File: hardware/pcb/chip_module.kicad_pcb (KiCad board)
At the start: 4 copper layers, 150 x 140 mm, 201 parts, among them J12 BTB_DAUGHTER

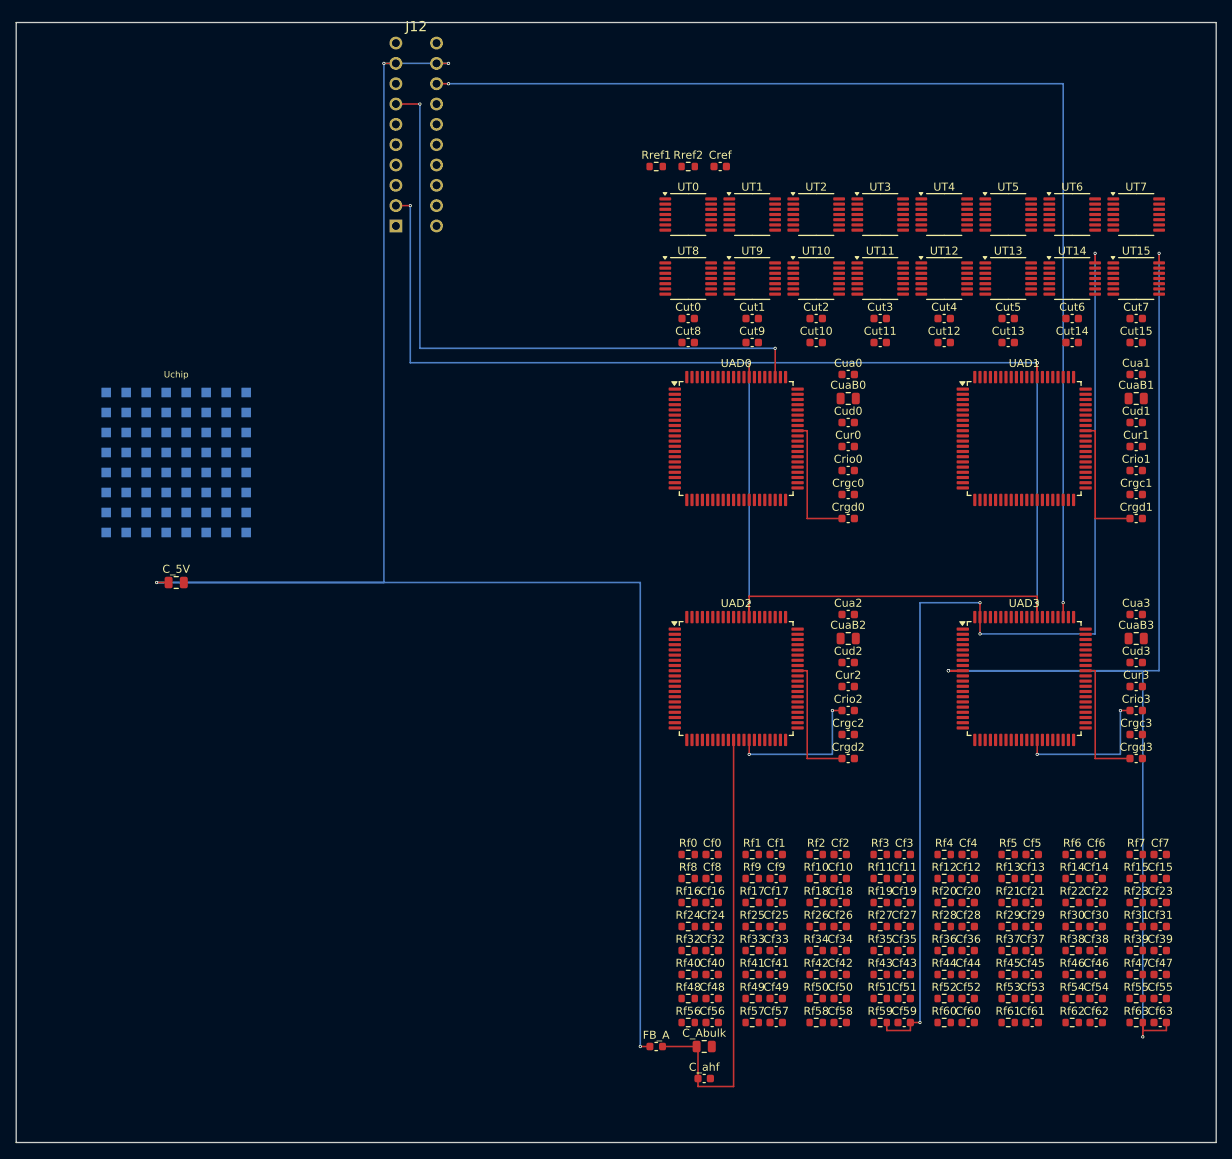
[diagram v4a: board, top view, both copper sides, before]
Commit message: route: 2.5mm dog-bone chip fanout (128 die vias) + planes poured, DRC 0/0/0
_chip_fanout was a no-op deferring all 128 die nets to FreeRouting, which
plateaued (~474 unrouted). Restore a real dog-bone fanout for the 2.5 mm 8x8
die grid: 0.15 mm stub on the pad's own layer + 0.20 mm through-via 1.0 mm out
(in the 1.3 mm inter-pad gap), escaped on the opposite clear surface by the
line router. At 2.5 mm pitch the via clears adjacent pads by 0.80 mm -- the
68/98 shorting_items of the old 0.30 mm design cannot occur. The fixed 3 mm
escape that shorted adjacent-row escapes on the same column is GONE; the line
router routes via->target on the clear layer (marking keepout, no overlaps).

EM_ANODE (+12V_EMIT) is left to the power router. Planes poured on both boards
(GND + +3V3 zones). Both boards DRC 0 violations / 0 unconnected / 0 shorts.

Via->target closure for the 64 emitter_cat (main) + 64 DET_IN (head) + 64
DET_TIA (head) is still pending -- the line router cannot place 64 long
single-layer crossings; FreeRouting closes the reduced problem next.

Co-Authored-By: Claude Code <noreply@anthropic.com>
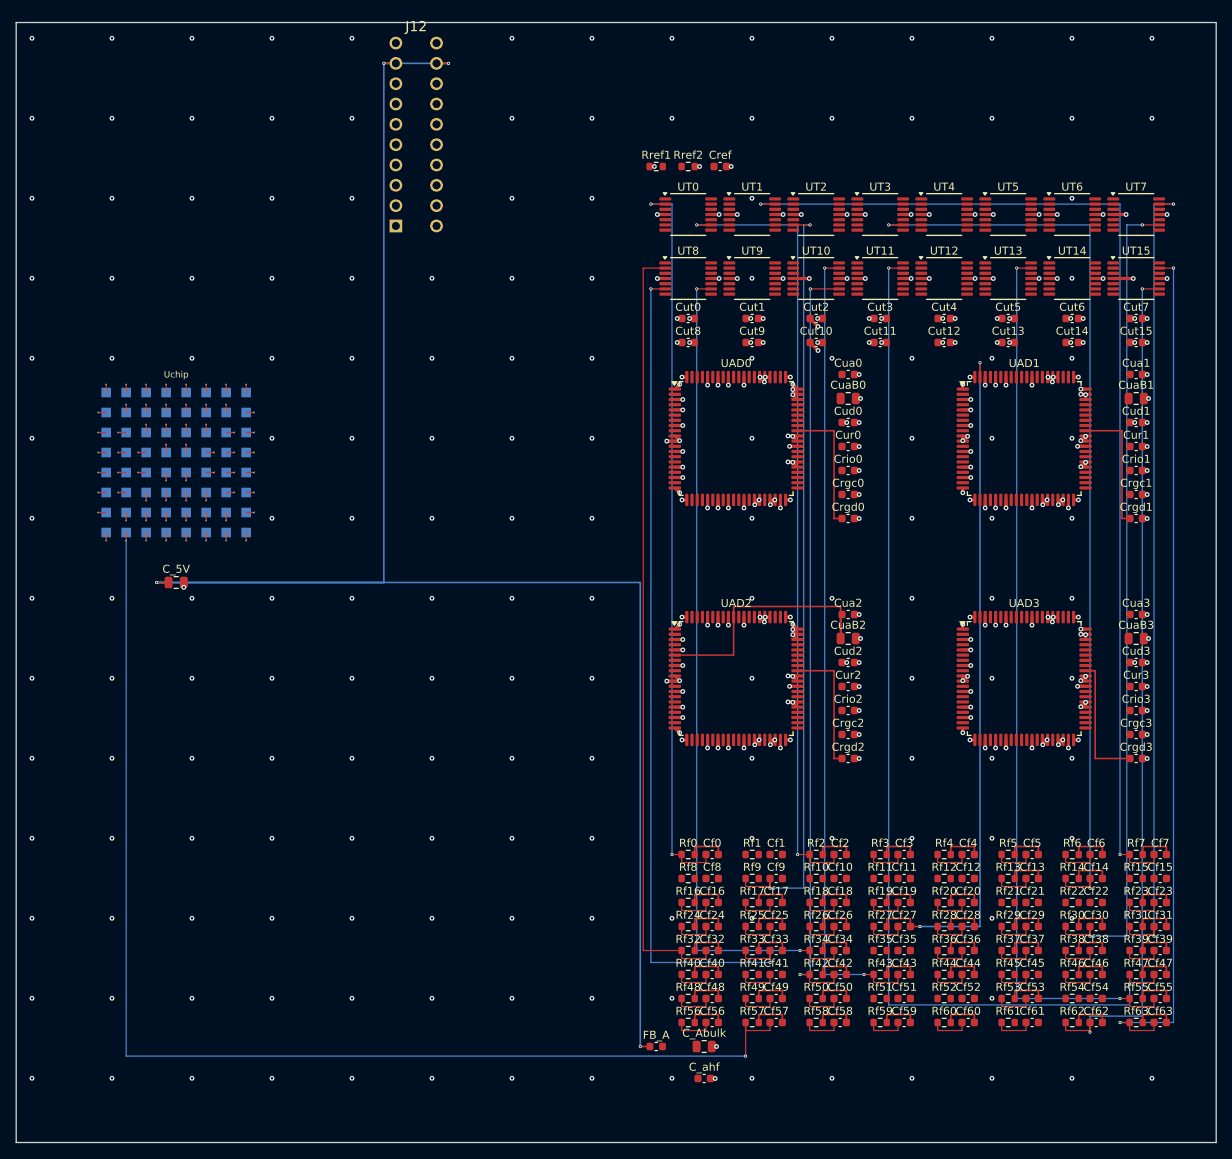
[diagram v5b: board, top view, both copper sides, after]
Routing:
- net adc_convst: track 210.0 -> 0.00 mm, vias 6 -> 0
- net GND: track 0.00 -> 161.7 mm, vias 0 -> 368
- net DET_TIA63: track 160.1 -> 4.95 mm, vias 4 -> 0
- net DET_IN57: track 0.00 -> 152.1 mm, vias 0 -> 2
- net adc_cs3: track 145.0 -> 0.00 mm, vias 2 -> 0
- net DET_IN7: track 0.00 -> 135.3 mm, vias 0 -> 3
- net DET_IN47: track 0.00 -> 133.9 mm, vias 0 -> 3
- net DET_TIA59: track 133.2 -> 4.95 mm, vias 4 -> 0
- net DET_IN14: track 0.00 -> 117.1 mm, vias 0 -> 3
- net DET_IN55: track 0.00 -> 113.3 mm, vias 0 -> 3
- net DET_IN63: track 0.00 -> 110.0 mm, vias 0 -> 3
- net DET_IN62: track 0.00 -> 108.8 mm, vias 0 -> 3
- net DET_IN33: track 0.00 -> 108.4 mm, vias 0 -> 3
- net DET_IN30: track 0.00 -> 104.8 mm, vias 0 -> 3
- net DET_IN34: track 0.00 -> 104.7 mm, vias 0 -> 3
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- added copper zone on In2.Cu, net +3V3
- added copper zone on In1.Cu, net GND

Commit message: route: fix flipped-footprint pad layer (cu_layers) + re-pour head planes
The head board's Uchip die footprint is flipped (IsFlipped, on B.Cu).
p.GetLayer() returns 0 (F.Cu) for pads on a flipped footprint even though
their real layer set is [31,38] = B.Cu+B.Mask, so the dog-bone stubs were
placed on F.Cu -- disconnected from the B.Cu die pads (die pads floating).

Fix: derive the real pad copper layers from GetLayerSet().Seq() filtered to
copper (<=31), stored on _PadProxy.cu_layers. _chip_fanout picks pad_lay
from cu_layers (F.Cu if present, else B.Cu); _pad_layers uses cu_layers for
the obstacle map so the router guards the real B.Cu die pads. Synthetic
via_pads pass cu_layers=[esc_lay].

Re-poured the head planes (route_qssc_pcb) to carve fresh anti-pads around
the corrected B.Cu stubs/vias -- the prior GND fill was stale (poured around
the old wrong-layer F.Cu stubs), shorting DET_IN to GND.

Result: BOTH boards DRC 0/0/0 (0 violations, 0 unconnected).
Adds tests/test_pcb_connectivity.py -- the real connectivity bar: a
graph-connectivity union-find test that catches split nets (a half-routed
die net: dog-bone via placed but never closed to the TLC5947/TIA target).
Fails by design until routing completes -- the post-routing gate.

Co-Authored-By: Claude Code <noreply@anthropic.com>
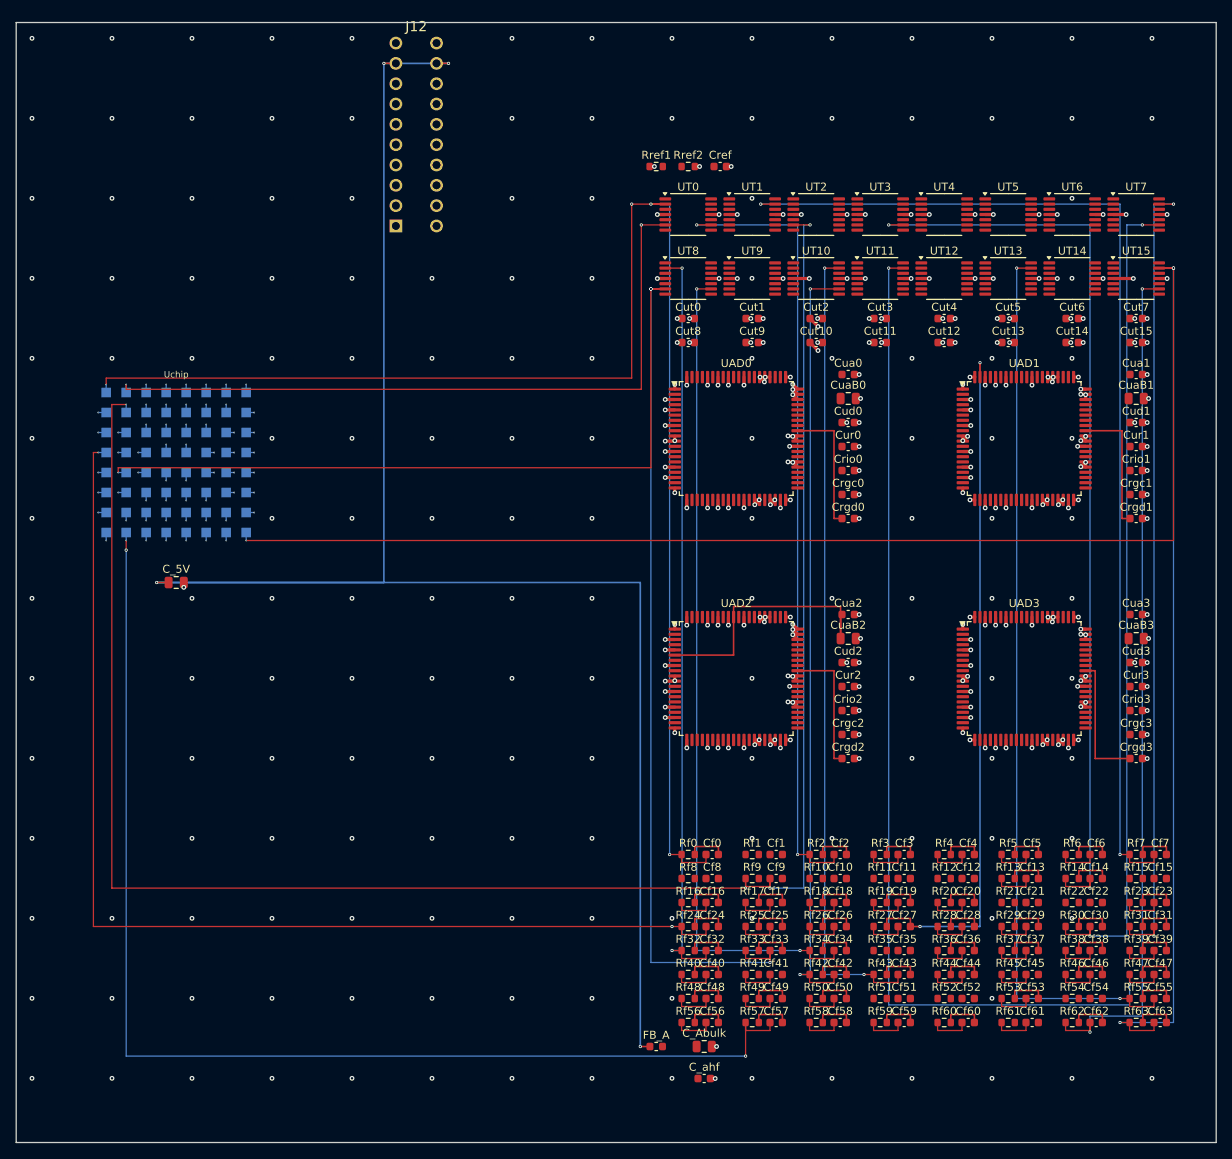
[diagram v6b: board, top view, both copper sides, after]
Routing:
- net DET_IN63: track 110.0 -> 261.8 mm, vias 3 -> 4
- net DET_IN9: track 97.3 -> 239.9 mm, vias 3 -> 4
- net DET_IN24: track 6.05 -> 139.4 mm, vias 1 -> 2
- net DET_IN0: track 93.0 -> 185.4 mm, vias 3 -> 4
- net DET_IN33: track 108.4 -> 199.8 mm, vias 3 -> 4
- net DET_IN1: track 1.00 -> 89.5 mm, vias 1 -> 2
- net DET_IN32: track 98.9 -> 95.9 mm, vias 1 -> 3
- net GND: track 161.7 -> 164.6 mm, vias 368 -> 364
- net DET_IN57: vias 2 -> 3

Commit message: head: bump detector head to 6 layers (4 signal layers for the die bus)
The 4-layer head put the 64-net die bus (DET_IN + DET_TIA) on only 2 signal
layers (F.Cu/B.Cu), at the autorouter's density ceiling.  6 layers add
In3.Cu + In4.Cu signal layers so route_signals + FreeRouting have 4 signal
layers (F.Cu/In3.Cu/In4.Cu/B.Cu).  route_signals.build() auto-selects the
4-signal-layer set from GetCopperLayerCount() (>4 branch), no router edit
needed; route_qssc_pcb reads plane labels dynamically.  HEAD_STACK_UP is a
6-layer 1.6mm FR4 build (In1.Cu GND one 0.15mm prepreg below F.Cu for the
TIA->ADC analog reference).  Die Uchip 64 DET pads stay on B.Cu.

Main board (qssc.*) is regenerated too: the JTAG J9 pin-9 +3V3 (VREF) fix
now comes from the generator code (replacing the earlier surgical edit),
and the .kicad_pcb is re-serialised in generator format (cosmetic
normalisation -- no layout/net change).  ruff CI rule clean.

Co-Authored-By: Claude Code <noreply@anthropic.com>
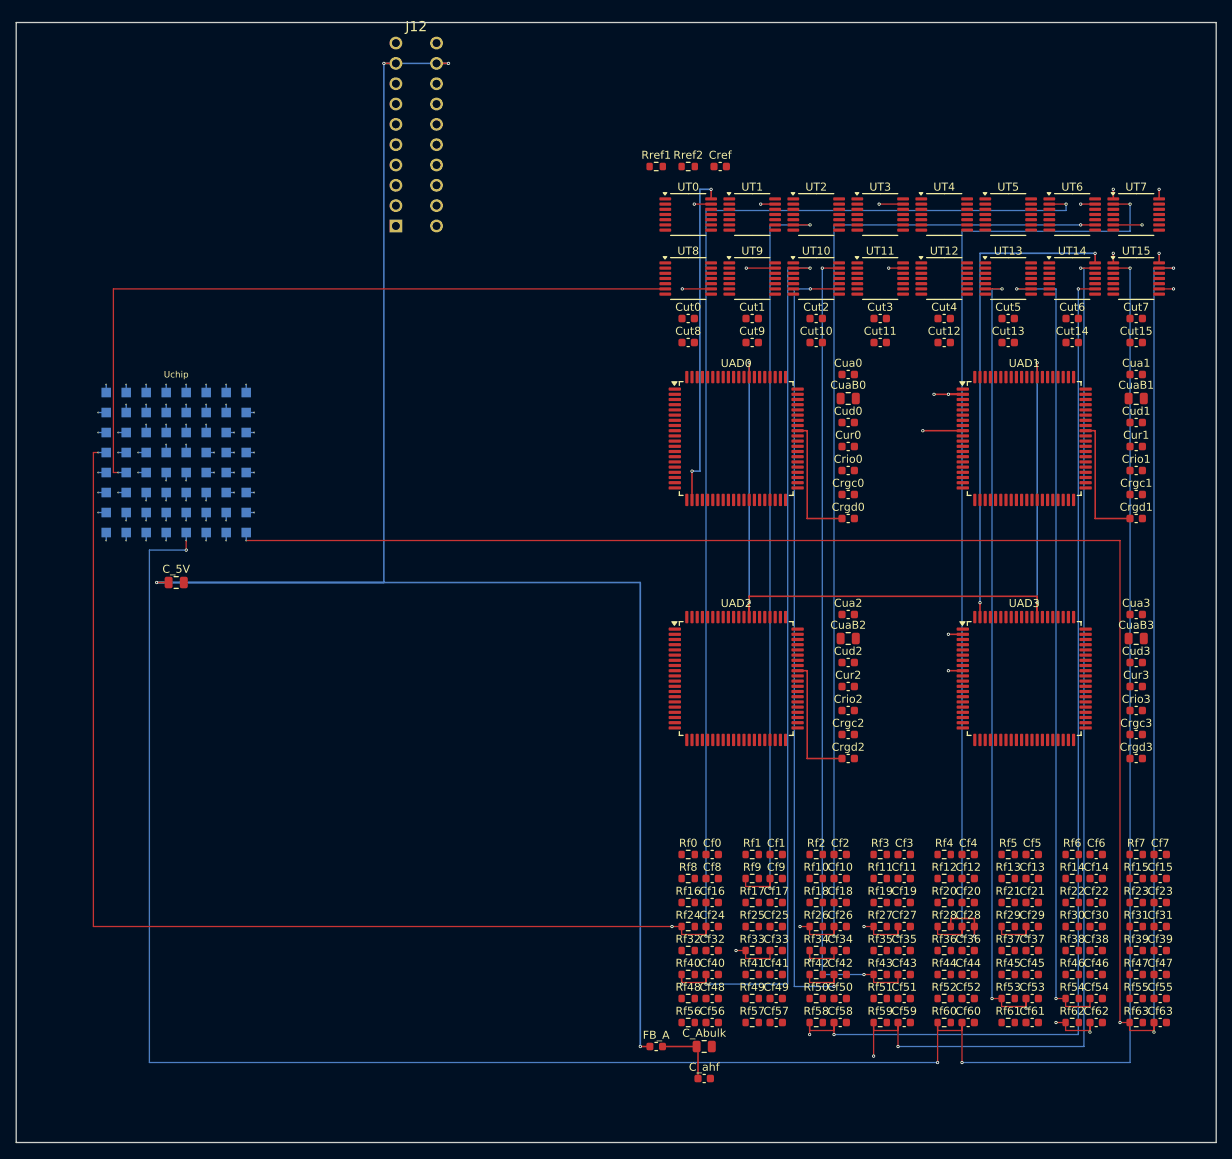
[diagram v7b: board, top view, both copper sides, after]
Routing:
- net DET_IN60: track 6.05 -> 306.8 mm, vias 1 -> 5
- net DET_IN59: track 6.05 -> 288.9 mm, vias 1 -> 4
- net DET_IN58: track 6.05 -> 279.6 mm, vias 1 -> 4
- net DET_IN27: track 6.05 -> 273.3 mm, vias 1 -> 4
- net DET_IN26: track 6.05 -> 272.0 mm, vias 1 -> 4
- net DET_IN53: track 6.05 -> 263.9 mm, vias 1 -> 4
- net DET_IN40: track 6.05 -> 247.4 mm, vias 1 -> 4
- net DET_IN0: track 185.4 -> 1.00 mm, vias 4 -> 1
- net DET_IN62: track 108.8 -> 277.6 mm, vias 3 -> 4
- net GND: track 164.6 -> 0.00 mm, vias 364 -> 0
- net DET_IN57: track 152.1 -> 1.00 mm, vias 3 -> 1
- net DET_IN34: track 104.7 -> 248.3 mm
- net DET_IN9: track 239.9 -> 97.3 mm, vias 4 -> 3
- net DET_IN24: track 139.4 -> 279.2 mm, vias 2 -> 4
- net DET_TIA28: track 4.95 -> 131.8 mm, vias 0 -> 4
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- removed copper zone on In2.Cu, net +3V3
- removed copper zone on In1.Cu, net GND
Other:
- copper layers 4 -> 6

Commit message: fix(detector): add DET_COMMON pad -> DET_REF, close the detector common electrode
The die TOP (detector) face had only 64 DET pixel pads -- the continuous
ITO common back-electrode (DET_COMMON, the shared detector masa per
FABRICATION_PROTOCOL_P0.md: 130 contacts = 64 DET + 64 EM-cathode + 2
ITO commons) was never contacted.  The TIA reference (DET_REF, 1.65 V
virtual ground) existed but had no bond point to the die ITO, so the
photodetector circuit was open on the bias/return side for all 64
graphene/MoS2 pixels.  The emitter face got its common (EM_ANODE); the
detector face did not -- that asymmetry is the defect.

Fix: add a DET_COMMON edge pad to chip_footprint_det() (B.Cu + B.Mask,
mirrors EM_ANODE on the emitter face) and map DET_COMMON -> DET_REF in
chip_net_map_det() + a DET_COMMON pin in chip_pin_list_det().  Zero-bias
short-circuit photocurrent readout (pads held at virtual ground, ITO at
the same 1.65 V -> ~0 V across the photodetector, max responsivity for
the photogating graphene/MoS2 detector; DET_REF only sets the DC
voltage, no net photocurrent flows through it).

route_signals dog-bones the new pad (65 detector-face fanout vias, was
64).  Also corrects stale '0.30 mm pitch' comments -> 2.5 mm (the die
is an 8x8 grid at 2.5 mm, 17.5 mm span on the 20 mm body; 1.2 mm pads
cannot exist at 0.30 mm pitch) and the '4-layer head' -> 6-layer note.
Main board unchanged (detector face is head-only).  ruff CI clean.

Co-Authored-By: Claude Code <noreply@anthropic.com>
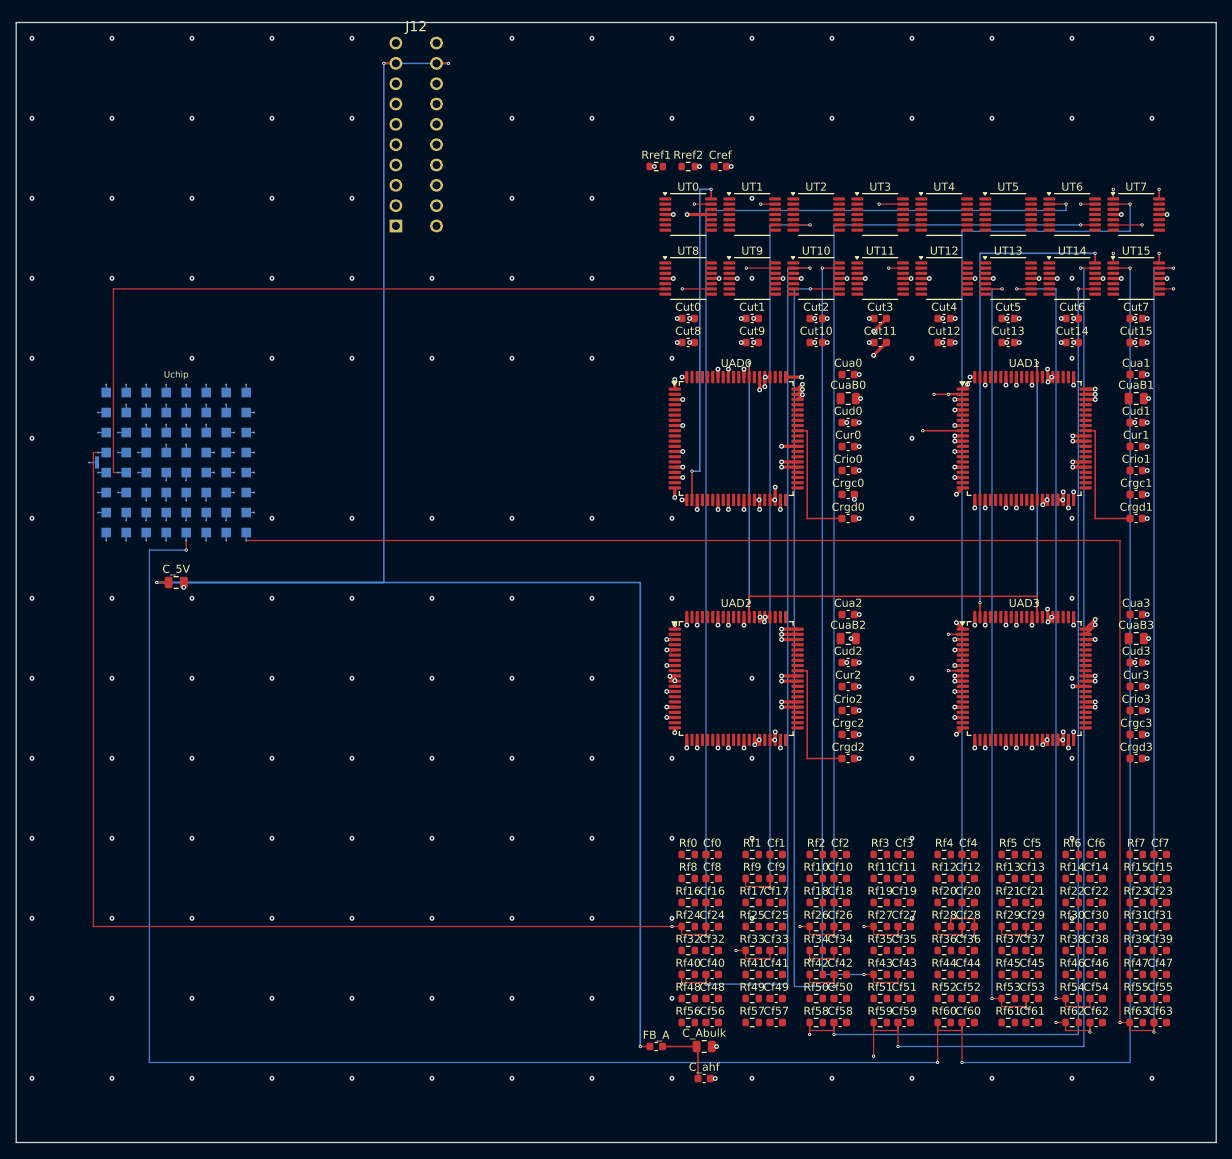
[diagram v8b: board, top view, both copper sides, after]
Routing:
- net GND: track 0.00 -> 184.6 mm, vias 0 -> 336
- net +3V3: track 0.00 -> 35.2 mm, vias 0 -> 43
- net DET_REF: track 0.00 -> 1.00 mm, vias 0 -> 1
- added copper zone on In2.Cu, net +3V3
- added copper zone on In1.Cu, net GND
